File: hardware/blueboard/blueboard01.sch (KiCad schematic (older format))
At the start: 135 parts, among them SW1 SW_SPST

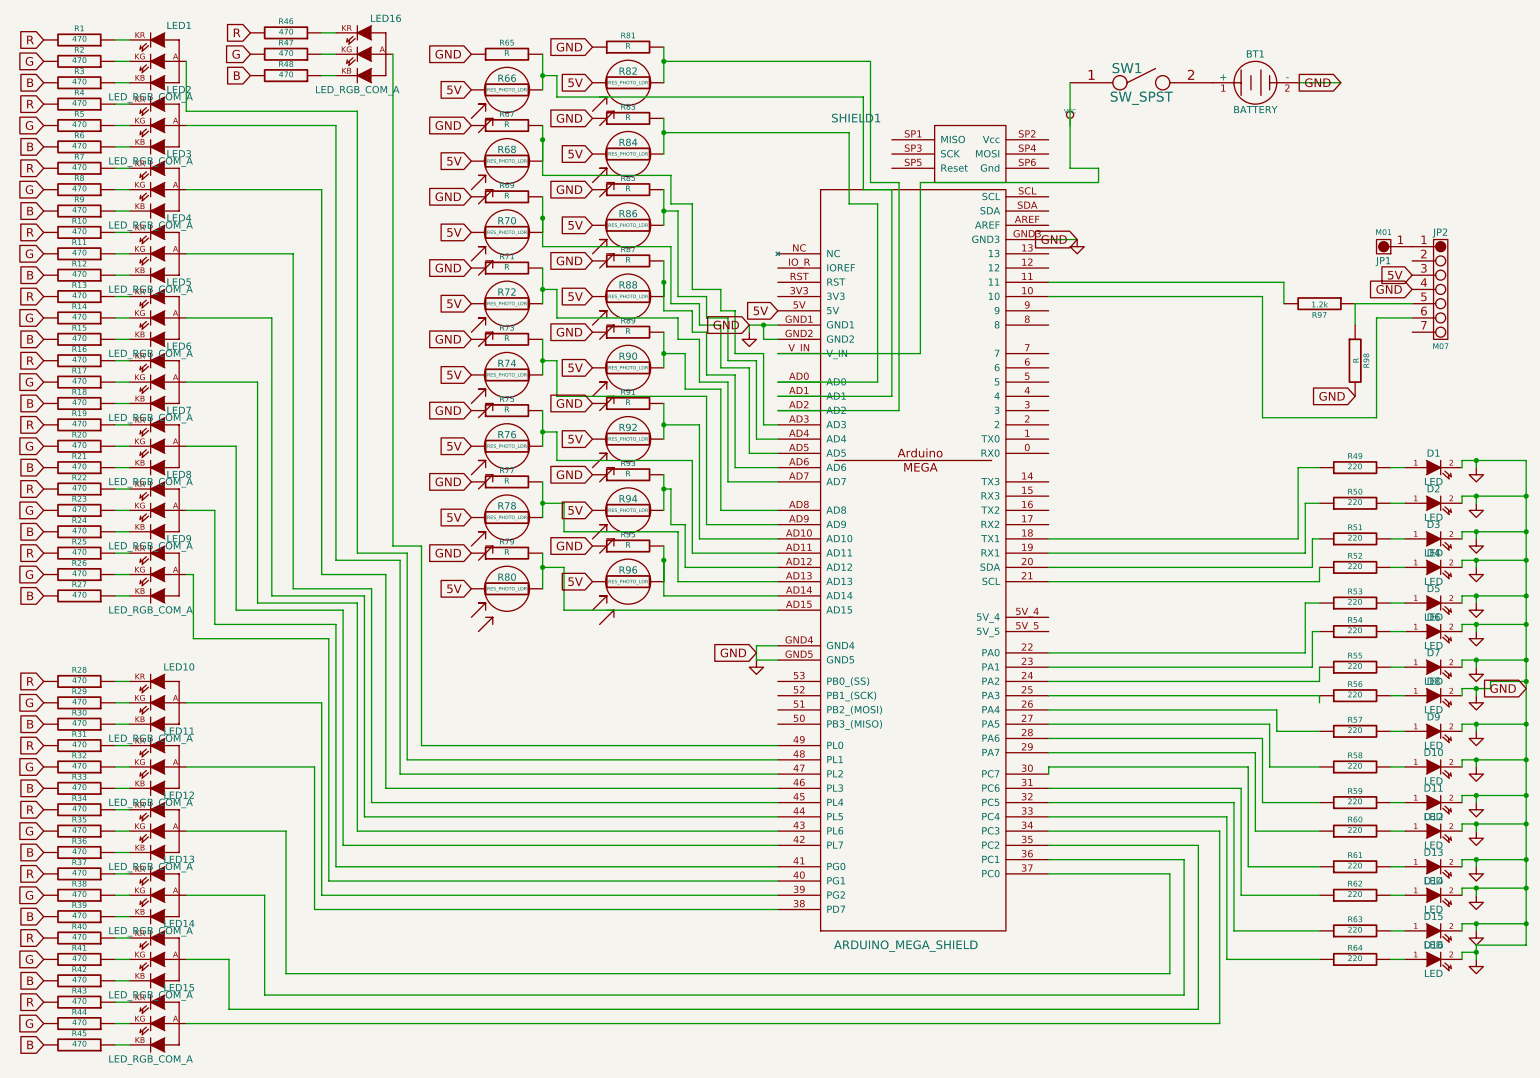
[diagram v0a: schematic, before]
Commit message: state when board was cncd
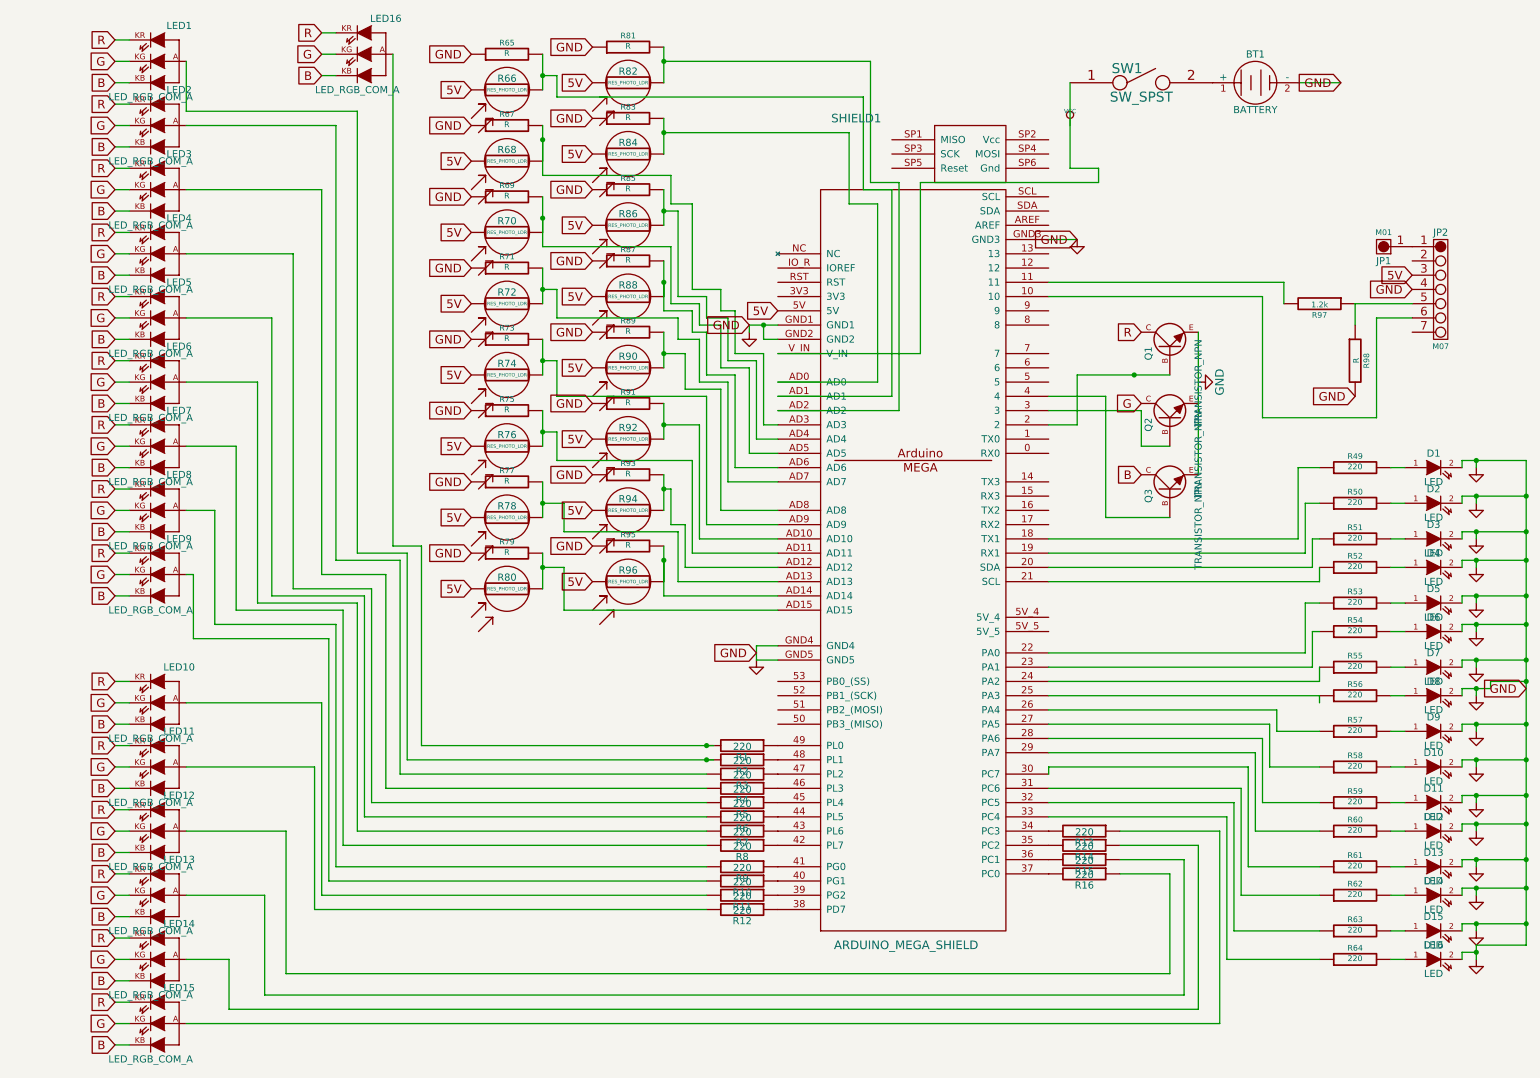
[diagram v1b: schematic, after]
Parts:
- removed R17, R18, R19, R20, R21, R22, R23, R24, R25, R26, R27, R28, R29, R30, R31, R32, R33, R34, R35, R36, R37, R38, R39, R40, R41, R42, R43, R44, R45, R46, R47, R48: 470, ~, symbol R
- added Q1, Q2, Q3: TRANSISTOR_NPN, symbol TRANSISTOR_NPN
- R1, R10, R11, R12, R13, R14, R15, R16, R2, R3, R4, R5, R6, R7, R8, R9: value 470 -> 220; footprint ~ -> (none)
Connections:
- net B: now also LED1.KB, LED10.KB, LED11.KB, LED12.KB, LED13.KB, LED14.KB, LED15.KB, LED16.KB, LED2.KB, LED3.KB, LED4.KB, LED5.KB, LED6.KB, LED7.KB, LED8.KB, LED9.KB, Q3.C; no longer R12.2, R15.2, R3.2, R6.2, R9.2
- net G: now also LED1.KG, LED10.KG, LED11.KG, LED12.KG, LED13.KG, LED14.KG, LED15.KG, LED16.KG, LED2.KG, LED3.KG, LED4.KG, LED5.KG, LED6.KG, LED7.KG, LED8.KG, LED9.KG, Q2.C; no longer R11.2, R14.2, R2.2, R5.2, R8.2
- net R: now also LED1.KR, LED10.KR, LED11.KR, LED12.KR, LED13.KR, LED14.KR, LED15.KR, LED16.KR, LED2.KR, LED3.KR, LED4.KR, LED5.KR, LED6.KR, LED7.KR, LED8.KR, LED9.KR, Q1.C; no longer R1.2, R10.2, R13.2, R16.2, R4.2, R7.2
- net at SHIELD1.2: now also Q1.B
- net at SHIELD1.3: now also Q2.B
- net at SHIELD1.34 (PC3): now also R13.2; no longer LED15.A
- net at SHIELD1.35 (PC2): now also R14.2; no longer LED14.A
- net at SHIELD1.36 (PC1): now also R15.2; no longer LED13.A
- net at SHIELD1.37 (PC0): now also R16.2; no longer LED12.A
- net at SHIELD1.38 (PD7): now also R12.1; no longer LED11.A
- net at SHIELD1.39 (PG2): now also R11.1; no longer LED10.A
- net at SHIELD1.4: now also Q3.B
- net at SHIELD1.40 (PG1): now also R10.1; no longer LED9.A
- net at SHIELD1.41 (PG0): now also R9.1; no longer LED8.A
- net at SHIELD1.42 (PL7): now also R8.1; no longer LED7.A
- net at SHIELD1.43 (PL6): now also R7.1; no longer LED6.A
- net at SHIELD1.44 (PL5): now also R6.1; no longer LED5.A
- net at SHIELD1.45 (PL4): now also R5.1; no longer LED4.A
- net at SHIELD1.46 (PL3): now also R4.1; no longer LED3.A
- net at SHIELD1.47 (PL2): now also R3.1; no longer LED2.A
- net at SHIELD1.48 (PL1): now also R2.1; no longer LED1.A
- net at SHIELD1.49 (PL0): now also R1.1; no longer LED16.A
- net at R16.1: now also LED12.A; no longer LED6.KR
- net at R15.1: now also LED13.A; no longer LED5.KB
- net at R14.1: now also LED14.A; no longer LED5.KG
- net at R13.1: now also LED15.A; no longer LED5.KR
- new net: LED16.A, R1.2
- new net: LED9.A, R10.2
- new net: LED11.A, R12.2
- new net: LED10.A, R11.2
- new net: LED6.A, R7.2
- new net: LED5.A, R6.2
- new net: LED8.A, R9.2
- new net: LED7.A, R8.2
- new net: LED2.A, R3.2
- new net: LED1.A, R2.2
- new net: LED4.A, R5.2
- new net: LED3.A, R4.2
- new net: Q1.E, Q3.E
